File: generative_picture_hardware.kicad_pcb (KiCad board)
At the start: 2 copper layers, 100 x 100 mm, 73 parts, among them J1 e_Paper_HAT, J2 Conn_ARM_JTAG_SWD_10, J3 USB_C_Receptacle_USB2.0, Q1 PMN48XP, Q2 DMG9926UDM, Q3 MBT3904DW1, SW1 SW_Push, SW2 SW_Push, U1 AP2112K-3.3, U2 ESP32-WROOM-32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

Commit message: Adds stitching vias
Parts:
- moved R6 1.25 mm to (121.0, 123.8), turned to 0 degrees
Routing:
- net GND: track 79.2 -> 85.4 mm, vias 54 -> 114

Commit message: Uses copper fills for the battery power traces
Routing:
- net Net-(BT1-Pad2): track 36.5 -> 4.44 mm
- net GND: vias 114 -> 112
- added copper zone on F.Cu, net +BATT
- added copper zone on F.Cu, net Net-(BT1-Pad1)
- added copper zone on F.Cu, net Net-(BT1-Pad2)
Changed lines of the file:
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@@
   (segment (start 115.0625 96.1875) (end 116 95.25) (width 0.5) (layer "F.Cu") (net 1))
   (segment (start 116 95.25) (end 116 94.15) (width 0.5) (layer "F.Cu") (net 1))
-  (segment (start 113.5 94.75) (end 113.5 86.75) (width 0.5) (layer "F.Cu") (net 1))
-  (segment (start 109.95 105.26) (end 107.76 105.26) (width 0.5) (layer "F.Cu") (net 1))
-  (segment (start 114.475 85.775) (end 116.2 85.775) (width 0.5) (layer "F.Cu") (net 1))
-  (segment (start 110.05 98.2) (end 112.3 98.2) (width 0.5) (layer "F.Cu") (net 1))
   (segment (start 115.0625 98.2) (end 115.0625 96.1875) (width 0.5) (layer "F.Cu") (net 1))
-  (segment (start 112.3 98.2) (end 115.0625 98.2) (width 0.5) (layer "F.Cu") (net 1))
-  (segment (start 113.5 86.75) (end 114.475 85.775) (width 0.5) (layer "F.Cu") (net 1))
-  (segment (start 110.05 98.2) (end 113.5 94.75) (width 0.5) (layer "F.Cu") (net 1))
-  (segment (start 106.75 104.25) (end 106.75 101.5) (width 0.5) (layer "F.Cu") (net 1))
-  (segment (start 107.76 105.26) (end 106.75 104.25) (width 0.5) (layer "F.Cu") (net 1))
-  (segment (start 106.75 101.5) (end 110.05 98.2) (width 0.5) (layer "F.Cu") (net 1))
   (segment (start 115.74 103.26) (end 115.75 103.25) (width 0.5) (layer "F.Cu") (net 2))
   (segment (start 109.95 103.26) (end 115.74 103.26) (width 0.5) (layer "F.Cu") (net 2))
@@
   (via (at 118 84) (size 0.8) (drill 0.4) (layers "F.Cu" "B.Cu") (net 3))
   (via (at 163.5 121) (size 0.8) (drill 0.4) (layers "F.Cu" "B.Cu") (free) (net 3))
-  (via (at 115 90) (size 0.8) (drill 0.4) (layers "F.Cu" "B.Cu") (free) (net 3))
   (via (at 188.5 120.5) (size 0.8) (drill 0.4) (layers "F.Cu" "B.Cu") (free) (net 3))
   (via (at 172.449748 116.949748) (size 0.8) (drill 0.4) (layers "F.Cu" "B.Cu") (free) (net 3))
@@
   (via (at 145.4 115) (size 0.8) (drill 0.4) (layers "F.Cu" "B.Cu") (net 3))
   (via (at 172.449748 56.949748) (size 0.8) (drill 0.4) (layers "F.Cu" "B.Cu") (free) (net 3))
-  (via (at 122.449748 116.949748) (size 0.8) (drill 0.4) (layers "F.Cu" "B.Cu") (free) (net 3))
   (via (at 157.449748 66.949748) (size 0.8) (drill 0.4) (layers "F.Cu" "B.Cu") (free) (net 3))
   (via (at 137.5 118) (size 0.8) (drill 0.4) (layers "F.Cu" "B.Cu") (net 3))
@@
   (segment (start 127.2875 137.054098) (end 127.2875 135.516598) (width 0.5) (layer "F.Cu") (net 10))
   (segment (start 117.1375 98.2) (end 117.1375 93.62248) (width 0.5) (layer "F.Cu") (net 11))
-  (segment (start 117.1375 98.2) (end 120.1 98.2) (width 0.5) (layer "F.Cu") (net 11))
+  (segment (start 117.1375 98.2) (end 120.1 98.2) (width 1.5) (layer "F.Cu") (net 11))
   (segment (start 117.1375 93.62248) (end 116.76502 93.25) (width 0.5) (layer "F.Cu") (net 11))
   (segment (start 116.05 93.25) (end 116 93.2) (width 0.5) (layer "F.Cu") (net 11))
@@
   (segment (start 137.25 148.25) (end 137.252532 148.247468) (width 0.25) (layer "F.Cu") (net 12))
   (segment (start 139.55 148.612459) (end 139.55 149.102479) (width 0.25) (layer "F.Cu") (net 12))
-  (segment (start 141.220372 146.725) (end 143.43125 146.725) (width 0.25) (layer "F.Cu") (net 13))
+  (segment (start 139.727479 146.725) (end 139.55 146.902479) (width 0.25) (layer "F.Cu") (net 13))
   (segment (start 139.185009 147.75749) (end 139.55 147.392499) (width 0.25) (layer "F.Cu") (net 13))
-  (segment (start 143.43125 146.725) (end 144.36875 145.7875) (width 0.25) (layer "F.Cu") (net 13))
   (segment (start 136.75 147.75) (end 136.75749 147.75749) (width 0.25) (layer "F.Cu") (net 13))
-  (segment (start 139.55 146.902479) (end 141.042893 146.902479) (width 0.25) (layer "F.Cu") (net 13))
   (segment (start 130.353554 147.75) (end 136.75 147.75) (width 0.25) (layer "F.Cu") (net 13))
   (segment (start 129.90002 144.704118) (end 129.99 144.794098) (width 0.25) (layer "F.Cu") (net 13))
@@
   (segment (start 129.49 145.851598) (end 129.49 146.886446) (width 0.25) (layer "F.Cu") (net 13))
   (segment (start 146.35625 145.7875) (end 144.36875 145.7875) (width 0.25) (layer "F.Cu") (net 13))
-  (segment (start 141.042893 146.902479) (end 141.220372 146.725) (width 0.25) (layer "F.Cu") (net 13))
   (segment (start 129.59998 144.704118) (end 129.90002 144.704118) (width 0.25) (layer "F.Cu") (net 13))
   (segment (start 136.75749 147.75749) (end 139.185009 147.75749) (width 0.25) (layer "F.Cu") (net 13))
   (segment (start 129.49 146.886446) (end 130.353554 147.75) (width 0.25) (layer "F.Cu") (net 13))
+  (segment (start 143.43125 146.725) (end 139.727479 146.725) (width 0.25) (layer "F.Cu") (net 13))
   (segment (start 129.99 144.794098) (end 129.99 145.851598) (width 0.25) (layer "F.Cu") (net 13))
   (segment (start 147.31875 145.8) (end 146.36875 145.8) (width 0.25) (layer "F.Cu") (net 13))
@@
   (segment (start 146.36875 145.8) (end 146.35625 145.7875) (width 0.25) (layer "F.Cu") (net 13))
   (segment (start 147.36875 145.75) (end 147.31875 145.8) (width 0.25) (layer "F.Cu") (net 13))
+  (segment (start 144.36875 145.7875) (end 143.43125 146.725) (width 0.25) (layer "F.Cu") (net 13))
   (segment (start 157.4925 140.55) (end 157.4925 139.3625) (width 0.25) (layer "F.Cu") (net 14))
   (segment (start 154.94 145.7025) (end 154.94 144.55) (width 0.25) (layer "F.Cu") (net 14))
@@
   (segment (start 187.175 146.575) (end 187.175 144.499748) (width 0.25) (layer "F.Cu") (net 83))
   (segment (start 161.8 144.55) (end 165.25 148) (width 0.25) (layer "F.Cu") (net 83))
+  (zone (net 8) (net_name "+BATT") (layer "F.Cu") (hatch edge 0.508)
+    (priority 1)
+    (connect_pads yes (clearance 0.508))
+    (min_thickness 0.254) (filled_areas_thickness no)
+    (fill yes (thermal_gap 0.508) (thermal_bridge_width 0.508))
+    (polygon
+      (pts
+        (xy 117 115.25)
+        (xy 125.25 115.25)
+        (xy 129.25 119.5)
+        (xy 129.25 126.25)
+        (xy 127.5 126.25)
+        (xy 127 125.75)
+        (xy 127 119.75)
+        (xy 124.5 117)
+        (xy 116.5 117)
+        (xy 116.5 114.75)
+      )
+    )
+  )
+  (zone (net 8) (net_name "+BATT") (layer "F.Cu") (hatch edge 0.508)
+    (priority 1)
+    (connect_pads yes (clearance 0.508))
+    (min_thickness 0.254) (filled_areas_thickness no)
+    (fill yes (thermal_gap 0.508) (thermal_bridge_width 0.508))
+    (polygon
+      (pts
+        (xy 123.75 97.25)
+        (xy 123.75 102.75)
+        (xy 119.25 107.25)
+        (xy 117 107.25)
+        (xy 116.5 107.75)
+        (xy 116.5 120)
+        (xy 116.25 120.5)
+        (xy 116.25 122)
+        (xy 116.25 122.5)
+        (xy 115.25 122.5)
+        (xy 114.75 122)
+        (xy 114.75 120)
+        (xy 114.75 105.5)
+        (xy 115.25 105)
+        (xy 118.25 105)
+        (xy 121 102.25)
+        (xy 121 97.25)
+        (xy 121.5 96.75)
+        (xy 123.25 96.75)
+      )
+    )
+  )
+  (zone (net 1) (net_name "Net-(BT1-Pad2)") (layer "F.Cu") (hatch edge 0.508)
+    (priority 1)
+    (connect_pads yes (clearance 0.508))
+    (min_thickness 0.254) (filled_areas_thickness no)
+    (fill yes (thermal_gap 0.508) (thermal_bridge_width 0.508))
+    (polygon
+      (pts
+        (xy 116.75 86.75)
+        (xy 115.25 86.75)
+        (xy 115.25 93.75)
+        (xy 116.75 93.75)
+        (xy 116.75 96.25)
+        (xy 116 97)
+        (xy 116 99)
+        (xy 115.5 99.5)
+        (xy 109.75 99.5)
+        (xy 107.5 101.25)
+        (xy 107.5 104.5)
+        (xy 112.25 104.5)
+        (xy 112.75 105)
+        (xy 112.75 105.75)
+        (xy 112.25 106.25)
+        (xy 106.75 106.25)
+        (xy 106.25 105.75)
+        (xy 106.25 98)
+        (xy 111.5 93)
+        (xy 111.5 85.25)
+        (xy 112 84.75)
+        (xy 116.25 84.75)
+        (xy 116.75 85.25)
+      )
+    )
+  )
+  (zone (net 2) (net_name "Net-(BT1-Pad1)") (layer "F.Cu") (hatch edge 0.508)
+    (priority 1)
+    (connect_pads yes (clearance 0.508))
+    (min_thickness 0.254) (filled_areas_thickness no)
+    (fill yes (thermal_gap 0.508) (thermal_bridge_width 0.508))
+    (polygon
+      (pts
+        (xy 116.75 103.75)
+        (xy 112.625 103.75)
+        (xy 108.25 103.75)
+        (xy 108.25 102.5)
+        (xy 108.75 102)
+        (xy 116.25 102)
+        (xy 116.75 102.5)
+      )
+    )
+  )
   (zone (net 3) (net_name "GND") (layer "F.Cu") (hatch edge 0.508)
     (connect_pads (clearance 0.508))

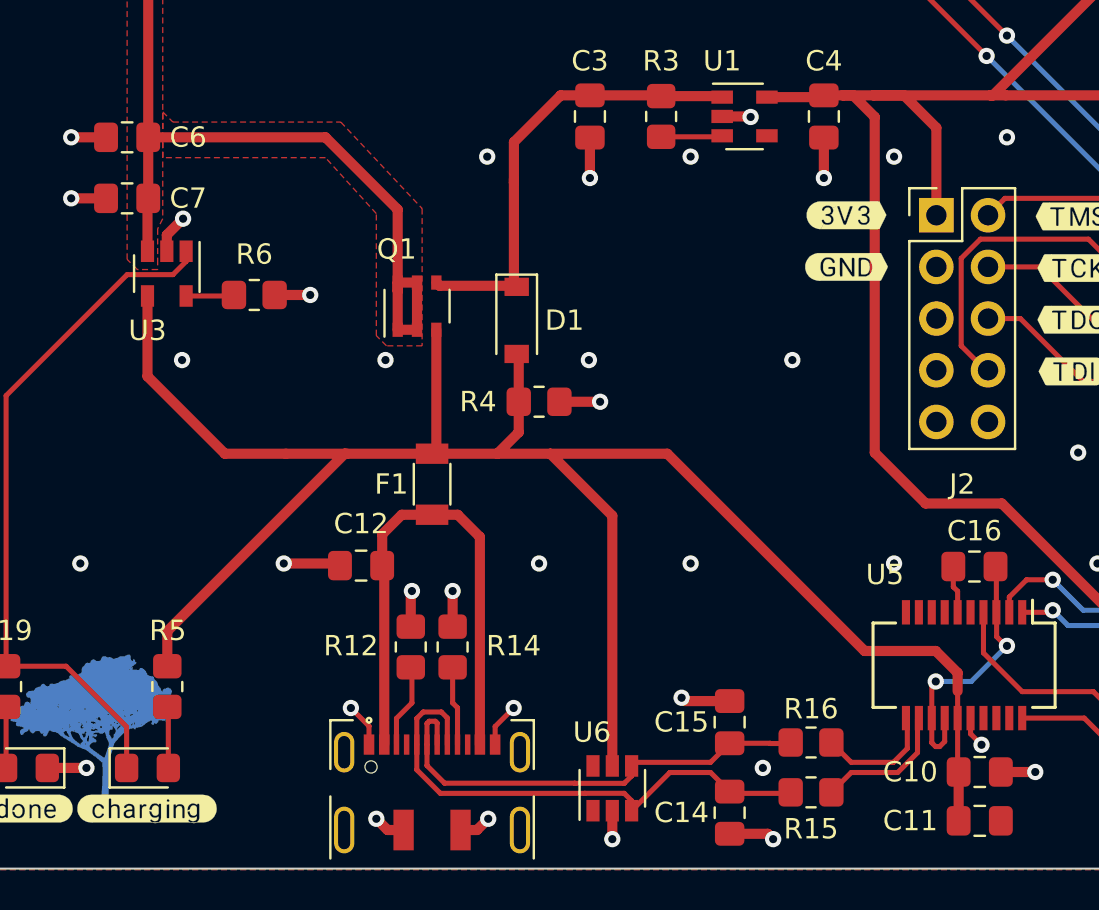
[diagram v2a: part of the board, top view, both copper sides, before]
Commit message: Uses copper fills for 5V rail
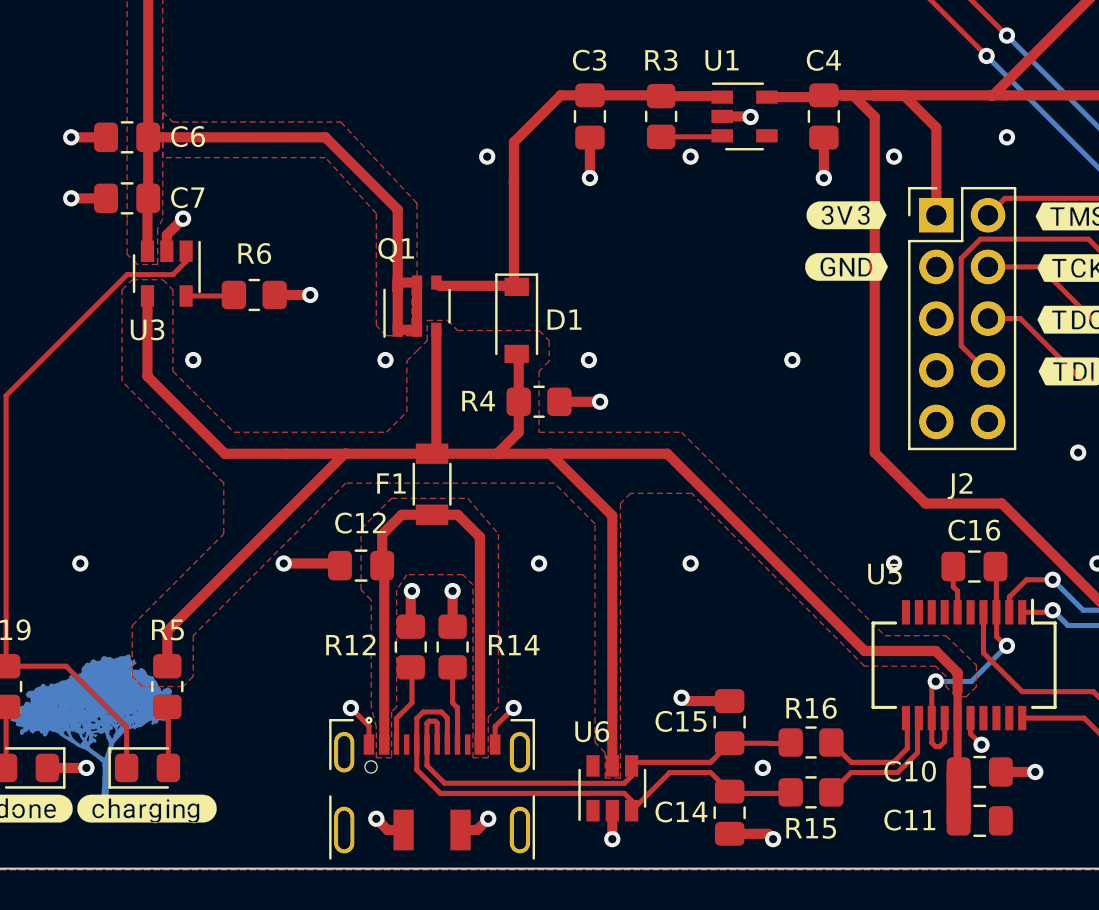
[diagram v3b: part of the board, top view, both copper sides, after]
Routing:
- added copper zone on F.Cu, net +5V
- added copper zone on F.Cu, net Net-(C12-Pad1)
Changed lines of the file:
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@@
   (via (at 174 94.25) (size 0.8) (drill 0.4) (layers "F.Cu" "B.Cu") (free) (net 3))
   (via (at 192.75 119.25) (size 0.8) (drill 0.4) (layers "F.Cu" "B.Cu") (net 3))
-  (via (at 117.449748 126.949748) (size 0.8) (drill 0.4) (layers "F.Cu" "B.Cu") (free) (net 3))
+  (via (at 118 126.949748) (size 0.8) (drill 0.4) (layers "F.Cu" "B.Cu") (free) (net 3))
   (via (at 147.449748 86.949748) (size 0.8) (drill 0.4) (layers "F.Cu" "B.Cu") (free) (net 3))
   (via (at 121.75 88.5) (size 0.8) (drill 0.4) (layers "F.Cu" "B.Cu") (net 3))
@@
   (segment (start 119.554098 131.554098) (end 115.75 127.75) (width 0.5) (layer "F.Cu") (net 9))
   (segment (start 129.74 131.554098) (end 122.554098 131.554098) (width 0.5) (layer "F.Cu") (net 9))
-  (segment (start 155.575 144.55) (end 155.575 147.15) (width 0.25) (layer "F.Cu") (net 9))
+  (segment (start 155.575 144.55) (end 155.575 147.15) (width 0.4) (layer "F.Cu") (net 9))
   (segment (start 138.6 134.6) (end 138.6 146.902479) (width 0.5) (layer "F.Cu") (net 9))
-  (segment (start 155.625 149.6) (end 155.625 147.2) (width 0.5) (layer "F.Cu") (net 9))
+  (segment (start 155.625 149.6) (end 155.625 147.2) (width 1.2) (layer "F.Cu") (net 9))
   (segment (start 122.554098 131.554098) (end 119.554098 131.554098) (width 0.5) (layer "F.Cu") (net 9))
   (segment (start 134 129) (end 134 126.75) (width 0.5) (layer "F.Cu") (net 9))
@@
   (segment (start 155.575 147.15) (end 155.625 147.2) (width 0.25) (layer "F.Cu") (net 9))
   (segment (start 132.945902 131.554098) (end 135.554098 131.554098) (width 0.5) (layer "F.Cu") (net 9))
-  (segment (start 155.575 144.55) (end 155.575 143.225) (width 0.25) (layer "F.Cu") (net 9))
+  (segment (start 155.575 144.55) (end 155.575 143.225) (width 0.4) (layer "F.Cu") (net 9))
   (segment (start 115.75 127.75) (end 115.75 123.8) (width 0.5) (layer "F.Cu") (net 9))
   (segment (start 151 141.25) (end 154.5 141.25) (width 0.5) (layer "F.Cu") (net 9))
@@
   (segment (start 187.175 146.575) (end 187.175 144.499748) (width 0.25) (layer "F.Cu") (net 83))
   (segment (start 161.8 144.55) (end 165.25 148) (width 0.25) (layer "F.Cu") (net 83))
+  (zone (net 10) (net_name "Net-(C12-Pad1)") (layer "F.Cu") (hatch edge 0.508)
+    (priority 1)
+    (connect_pads yes (clearance 0.508))
+    (min_thickness 0.254) (filled_areas_thickness no)
+    (fill yes (thermal_gap 0.508) (thermal_bridge_width 0.508))
+    (polygon
+      (pts
+        (xy 133 135.5)
+        (xy 133 144)
+        (xy 132.5 144.5)
+        (xy 132.5 146.5)
+        (xy 132 146.5)
+        (xy 131.75 146.5)
+        (xy 131.75 138)
+        (xy 131.25 137.5)
+        (xy 128.5 137.5)
+        (xy 128 138.25)
+        (xy 128 144)
+        (xy 127.75 144.25)
+        (xy 127.75 146.5)
+        (xy 127 146.5)
+        (xy 127 145)
+        (xy 126.75 144.002599)
+        (xy 126.75 138.75)
+        (xy 126.25 138.25)
+        (xy 126.25 135.25)
+        (xy 127.75 133.75)
+        (xy 131.5 133.75)
+      )
+    )
+  )
   (zone (net 8) (net_name "+BATT") (layer "F.Cu") (hatch edge 0.508)
     (priority 1)
@@
         (xy 117 115.25)
         (xy 125.25 115.25)
-        (xy 129.25 119.5)
-        (xy 129.25 126.25)
-        (xy 127.5 126.25)
-        (xy 127 125.75)
+        (xy 129 119.25)
+        (xy 129 122.75)
+        (xy 128.75 123)
+        (xy 128.75 125.75)
+        (xy 127.5 125.75)
+        (xy 127 125.25)
         (xy 127 119.75)
         (xy 124.5 117)
@@
         (xy 116.25 120.5)
         (xy 116.25 122)
-        (xy 116.25 122.5)
-        (xy 115.25 122.5)
-        (xy 114.75 122)
+        (xy 116.25 122.25)
+        (xy 115.25 122.25)
+        (xy 114.75 121.75)
         (xy 114.75 120)
         (xy 114.75 105.5)
@@
       )
     )
+  )
+  (zone (net 9) (net_name "+5V") (layer "F.Cu") (hatch edge 0.508)
+    (priority 1)
+    (connect_pads yes (clearance 0.508))
+    (min_thickness 0.254) (filled_areas_thickness no)
+    (fill yes (thermal_gap 0.508) (thermal_bridge_width 0.508))
+    (polygon
+      (pts
+        (xy 117 123.5)
+        (xy 117 127.5)
+        (xy 120 130.5)
+        (xy 127.5 130.5)
+        (xy 128.5 129.5)
+        (xy 128.5 127)
+        (xy 129 126.5)
+        (xy 129.5 126)
+        (xy 129.5 125)
+        (xy 130.5 125)
+        (xy 131 125.5)
+        (xy 135 125.5)
+        (xy 135.5 126)
+        (xy 135.5 127)
+        (xy 135 127.5)
+        (xy 135 130.5)
+        (xy 142 130.5)
+        (xy 152 140.5)
+        (xy 155 140.5)
+        (xy 156.5 141.95)
+        (xy 156.5 143)
+        (xy 156 143.5)
+        (xy 155.5 143.5)
+        (xy 155 143)
+        (xy 155 142.5)
+        (xy 154.5 142)
+        (xy 151 142)
+        (xy 142.5 133.5)
+        (xy 139.5 133.5)
+        (xy 139 134)
+        (xy 139 147.5)
+        (xy 138.25 147.5)
+        (xy 138.25 146.25)
+        (xy 137.75 145.75)
+        (xy 137.75 135)
+        (xy 135.75 133)
+        (xy 125.5 133)
+        (xy 118 140.5)
+        (xy 118 142.5)
+        (xy 117.5 143)
+        (xy 115.5 143)
+        (xy 115 142.5)
+        (xy 115 140)
+        (xy 119.5 135.5)
+        (xy 119.5 133)
+        (xy 114.5 128)
+        (xy 114.5 123.5)
+        (xy 115 123)
+        (xy 116.5 123)
+      )
+    )

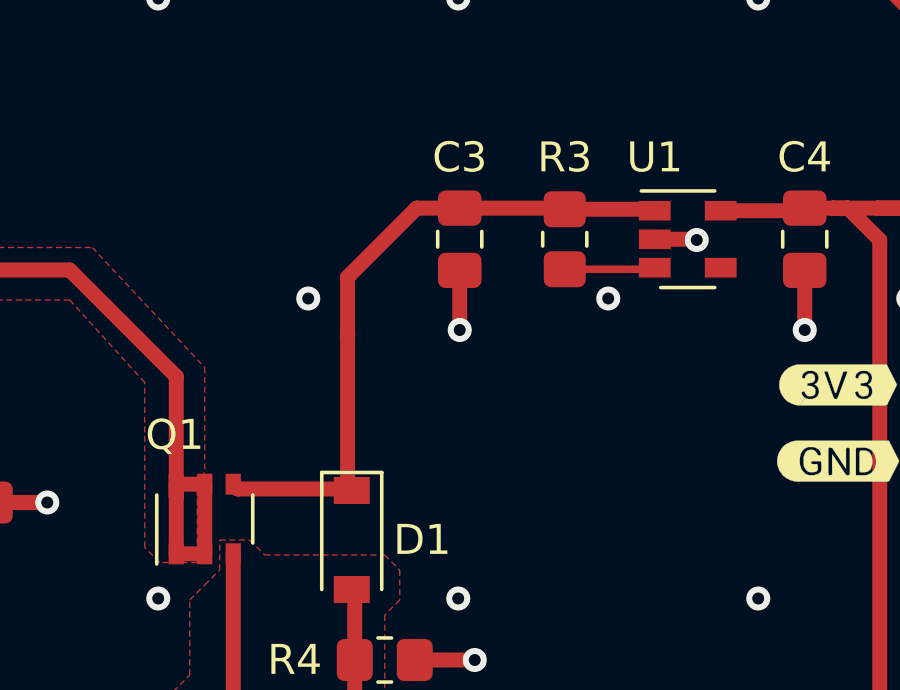
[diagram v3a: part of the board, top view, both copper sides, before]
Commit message: Uses copper fill for VCC path to regulator
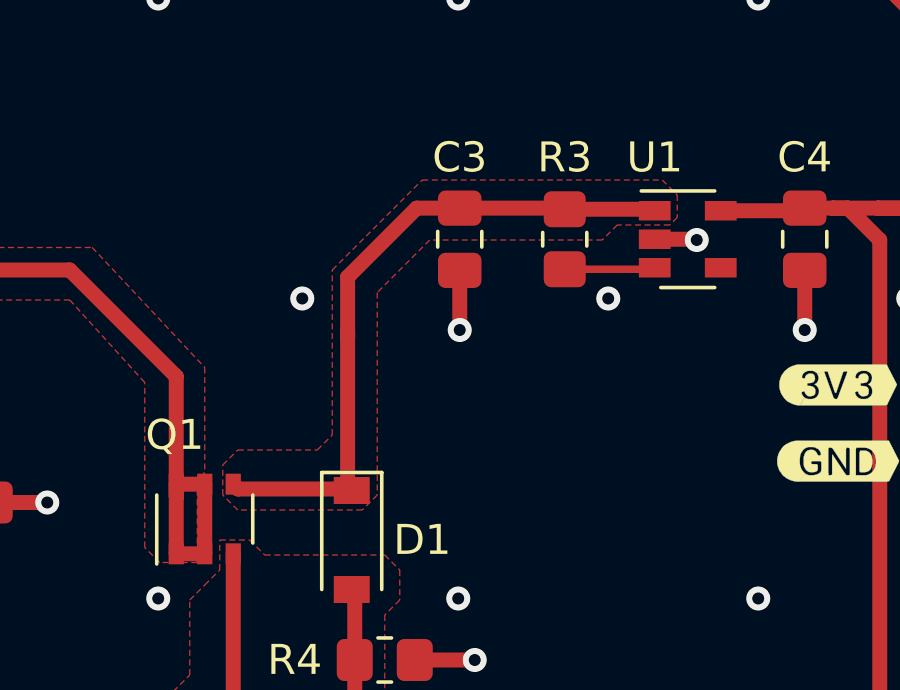
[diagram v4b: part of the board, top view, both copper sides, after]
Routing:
- added copper zone on F.Cu, net VCC
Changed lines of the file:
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@@
   (via (at 197.449748 106.949748) (size 0.8) (drill 0.4) (layers "F.Cu" "B.Cu") (free) (net 3))
   (via (at 112.449748 76.949748) (size 0.8) (drill 0.4) (layers "F.Cu" "B.Cu") (free) (net 3))
-  (via (at 132.449748 116.949748) (size 0.8) (drill 0.4) (layers "F.Cu" "B.Cu") (free) (net 3))
+  (via (at 132.25 116.949748) (size 0.8) (drill 0.4) (layers "F.Cu" "B.Cu") (free) (net 3))
   (via (at 127.449748 106.949748) (size 0.8) (drill 0.4) (layers "F.Cu" "B.Cu") (free) (net 3))
   (via (at 118 84) (size 0.8) (drill 0.4) (layers "F.Cu" "B.Cu") (net 3))
@@
     )
   )
+  (zone (net 6) (net_name "VCC") (layer "F.Cu") (hatch edge 0.508)
+    (priority 1)
+    (connect_pads (clearance 0.508))
+    (min_thickness 0.254) (filled_areas_thickness no)
+    (fill yes (thermal_gap 0.508) (thermal_bridge_width 0.508))
+    (polygon
+      (pts
+        (xy 144.75 113.5)
+        (xy 144.75 114.25)
+        (xy 144.5 114.5)
+        (xy 142.75 114.5)
+        (xy 142.25 115)
+        (xy 136.5 115)
+        (xy 134.75 116.75)
+        (xy 134.75 123.5)
+        (xy 134.25 124)
+        (xy 130.1 124)
+        (xy 129.6 123.5)
+        (xy 129.6 122.5)
+        (xy 130.1 122)
+        (xy 132.75 122)
+        (xy 133.25 121.5)
+        (xy 133.25 116)
+        (xy 136.25 113)
+        (xy 144.25 113)
+      )
+    )
+  )
   (zone (net 9) (net_name "+5V") (layer "F.Cu") (hatch edge 0.508)
     (priority 1)
-    (connect_pads yes (clearance 0.508))
+    (connect_pads (clearance 0.508))
     (min_thickness 0.254) (filled_areas_thickness no)
     (fill yes (thermal_gap 0.508) (thermal_bridge_width 0.508))
